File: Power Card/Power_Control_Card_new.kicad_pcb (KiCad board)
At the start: 2 copper layers, 100 x 62.5 mm, 29 parts, among them J4 Conn_01x04_Pin, Q1 FQPF27P06, Q2 FQPF27P06, U3 TSR2-2450, U4 TSR2-2433, U5 MCP9808_MSOP

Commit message: Changed Backplane and Power Card for proper connection between the killswitches in the new system
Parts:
- Q1, Q2: value FQPF27P06 -> IRF5305PbF
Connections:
- J2 pad B28: GND -> NJSW1
- J2 pad C27: NJSW1 -> SW2
- J2 pad C28: GND -> NJSW1
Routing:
- net NJSW1: track 91.6 -> 94.7 mm
- net SW2: track 82.2 -> 84.7 mm

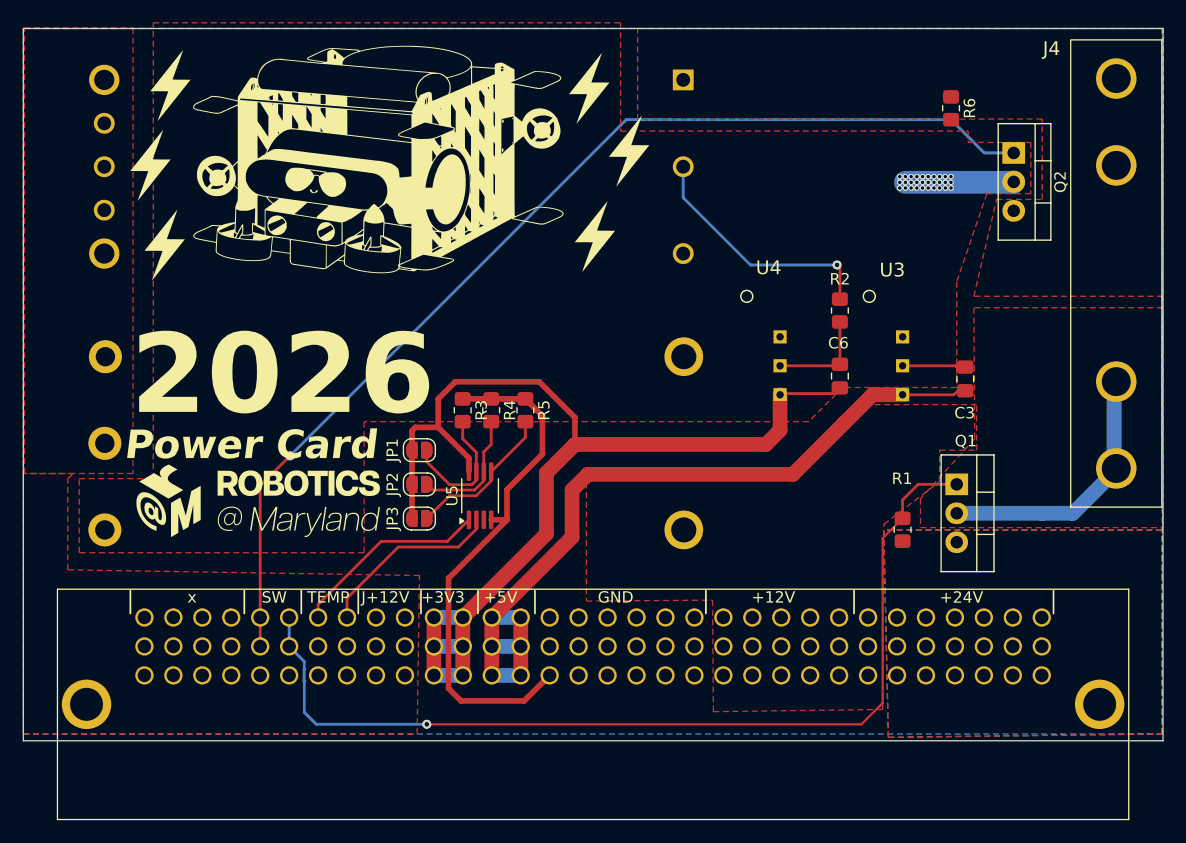
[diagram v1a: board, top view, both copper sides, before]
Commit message: added and fix temp sensor and error
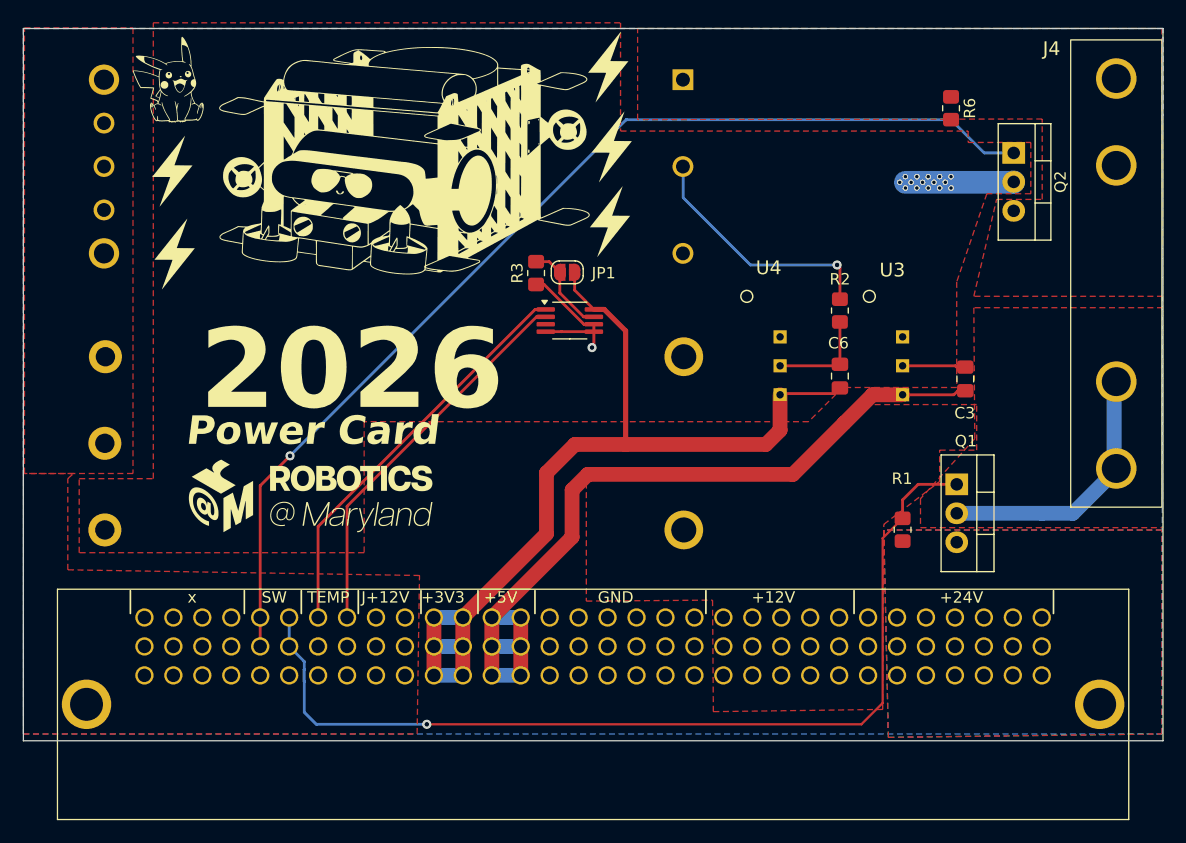
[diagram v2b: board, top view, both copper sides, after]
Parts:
- removed the G*** at (163.0, 54.0)
- removed JP2, JP3: SolderJumper_2_Open, Jumper:SolderJumper-2_P1.3mm_Open_RoundedPad1.0x1.5mm
- removed R4, R5: temp R, Resistor_SMD:R_0805_2012Metric_Pad1.20x1.40mm_HandSolder
- added G***: LOGO, Pikachu:Pikachu, F.Cu at (162.8, 54.2)
- moved JP1 20.3 mm to (197.8, 70.4), turned to 180 degrees
- moved U5 17.3 mm to (198.0, 74.6), turned to 0 degrees
- moved R3 13.7 mm to (195.1, 70.5), turned to 90 degrees
- moved G*** 4.62 mm to (175.1, 90.1)
- moved G*** 2.51 mm to (201.4, 52.4)
- moved G*** 2.29 mm to (179.4, 56.3)
- moved G*** 1.99 mm to (163.2, 61.5)
- moved G*** 1.86 mm to (201.6, 65.9)
- moved G*** 1.57 mm to (201.7, 59.4)
- moved G*** 1.17 mm to (163.4, 68.8)
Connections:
- U5 pad 5: Net-(JP3-B) -> GND
- U5 pad 6: Net-(JP2-B) -> GND
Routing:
- net GND: track 61.1 -> 27.4 mm, vias 0 -> 1
- net SDA2: track 17.5 -> 35.8 mm
- net SCL2: track 16.6 -> 34.3 mm
- net +3.3V: track 98.1 -> 81.7 mm
- net Net-(JP3-B): track 13.5 -> 0.00 mm
- net Net-(JP2-B): track 11.0 -> 0.00 mm
- net Net-(JP1-B): track 12.0 -> 8.14 mm
- net /NonJetsonPower: vias 30 -> 15

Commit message: actually connected the njsw1 resistor
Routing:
- net NJSW1: vias 1 -> 2
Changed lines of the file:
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@@
+	)
+	(segment
+		(start 231.5 57)
+		(end 228 57)
+		(width 0.25)
+		(layer "F.Cu")
+		(net 33)
 	)
 	(segment
@@
 	)
 	(segment
+		(start 234.42 59.92)
+		(end 231.5 57)
+		(width 0.25)
+		(layer "F.Cu")
+		(net 33)
+	)
+	(segment
 		(start 170.882617 100.682442)
 		(end 170.882617 103.222442)
@@
 		(start 170.882617 89.117383)
 		(end 170.882617 100.682442)
+		(width 0.25)
+		(layer "F.Cu")
+		(net 33)
+	)
+	(segment
+		(start 237 59.92)
+		(end 234.42 59.92)
 		(width 0.25)
 		(layer "F.Cu")
@@
 		(net 33)
 	)
-	(segment
-		(start 237 59.92)
-		(end 234.42 59.92)
-		(width 0.25)
-		(layer "B.Cu")
-		(net 33)
-	)
-	(segment
-		(start 234.42 59.92)
-		(end 231.5 57)
-		(width 0.25)
-		(layer "B.Cu")
-		(net 33)
-	)
-	(segment
-		(start 231.5 57)
-		(end 203 57)
+	(via
+		(at 228 57)
+		(size 0.8)
+		(drill 0.4)
+		(layers "F.Cu" "B.Cu")
+		(net 33)
+	)
+	(segment
+		(start 203 57)
+		(end 228 57)
 		(width 0.25)
 		(layer "B.Cu")
@@
 		(polygon
 			(pts
-				(xy 250 49) (xy 250.095918 72.5) (xy 233.5 72.5) (xy 235.5 64) (xy 239.5 64) (xy 239.5 56.940645)
-				(xy 204 57) (xy 204 49) (xy 235.5 49)
+				(xy 250 49) (xy 250.095918 72.5) (xy 233.5 72.5) (xy 235.5 64) (xy 242 64) (xy 242 55.452349) (xy 204 55.515884)
+				(xy 204 49) (xy 235.5 49)
 			)
 		)
@@
 		(polygon
 			(pts
-				(xy 202.5 48.5) (xy 202.5 58) (xy 233 58) (xy 233 59) (xy 238.5 59) (xy 238.5 63.5) (xy 234.641322 63.5)
+				(xy 202.5 48.5) (xy 202.5 56.5) (xy 233 56.5) (xy 241.5 56.5) (xy 241.5 63.5) (xy 234.641322 63.5)
 				(xy 232 71.231819) (xy 232 80.5) (xy 222 80.5) (xy 219 83.5) (xy 180 83.5) (xy 180 95) (xy 155 95)
 				(xy 155 88.5) (xy 161.5 88.5) (xy 161.5 48.5)
